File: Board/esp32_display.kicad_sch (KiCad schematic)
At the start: 1 part

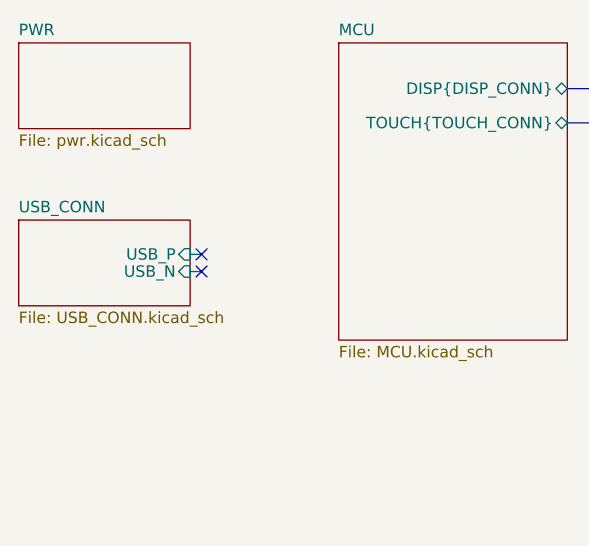
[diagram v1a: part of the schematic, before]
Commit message: Fix USB silkscreen over board warning, other minimal fixes
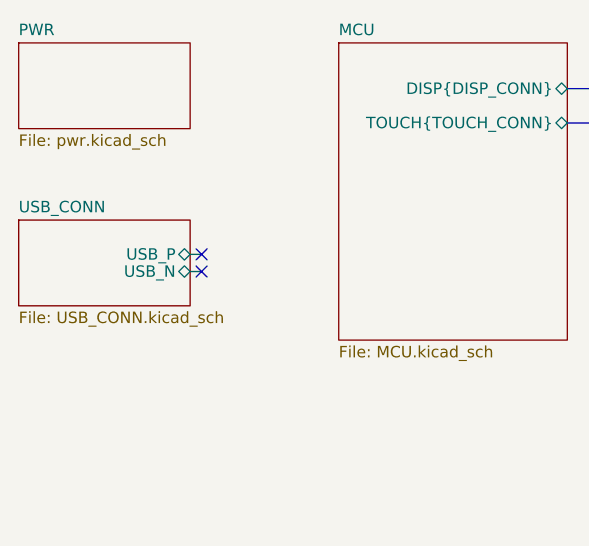
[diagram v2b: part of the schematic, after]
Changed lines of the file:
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@@
   (title_block
     (title "ESP32_display")
-    (date "2022/01/12")
+    (date "2022/01/17")
     (rev "v0.1")
     (company "Bzgec")
@@
       (effects (font (size 1.27 1.27)) (justify left top))
     )
-    (pin "USB_N" input (at 53.34 52.07 0)
+    (pin "USB_N" bidirectional (at 53.34 52.07 0)
       (effects (font (size 1.27 1.27)) (justify right))
     )
-    (pin "USB_P" input (at 53.34 50.165 0)
+    (pin "USB_P" bidirectional (at 53.34 50.165 0)
       (effects (font (size 1.27 1.27)) (justify right))
     )

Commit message: Add fiducials
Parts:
- added FID1, FID2, FID3: Fiducial, Fiducial:Fiducial_0.5mm_Mask1mm, symbol Mechanical:Fiducial
